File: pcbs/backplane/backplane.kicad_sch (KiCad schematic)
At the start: 138 parts, among them J1 Conn_01x02, J10 AFBR-2624Z, J11 AFBR-2624Z, J12 AFBR-1624Z, J14 Conn_01x02, J17 Conn_01x02, J19 Conn_01x02, J22 Conn_01x02, J24 Conn_01x02, J27 Conn_01x02, J29 Conn_01x02, J32 Conn_01x02, J34 Conn_01x02, J37 Conn_01x02, J39 Conn_01x02, J42 Conn_01x02, J44 Conn_01x02, J47 Conn_01x02, J48 Conn_01x02, J5 AFBR-2624Z, J8 Conn_01x02, J9 AFBR-2624Z, Q12 MMBT3904, Q13 MMBT3904, U11 AFBR-5972Z, U27 74LVC1G14, U29 74LVC1G14, U30 74LVC1G14, U32 LMV331, U7 FIN1019MTC

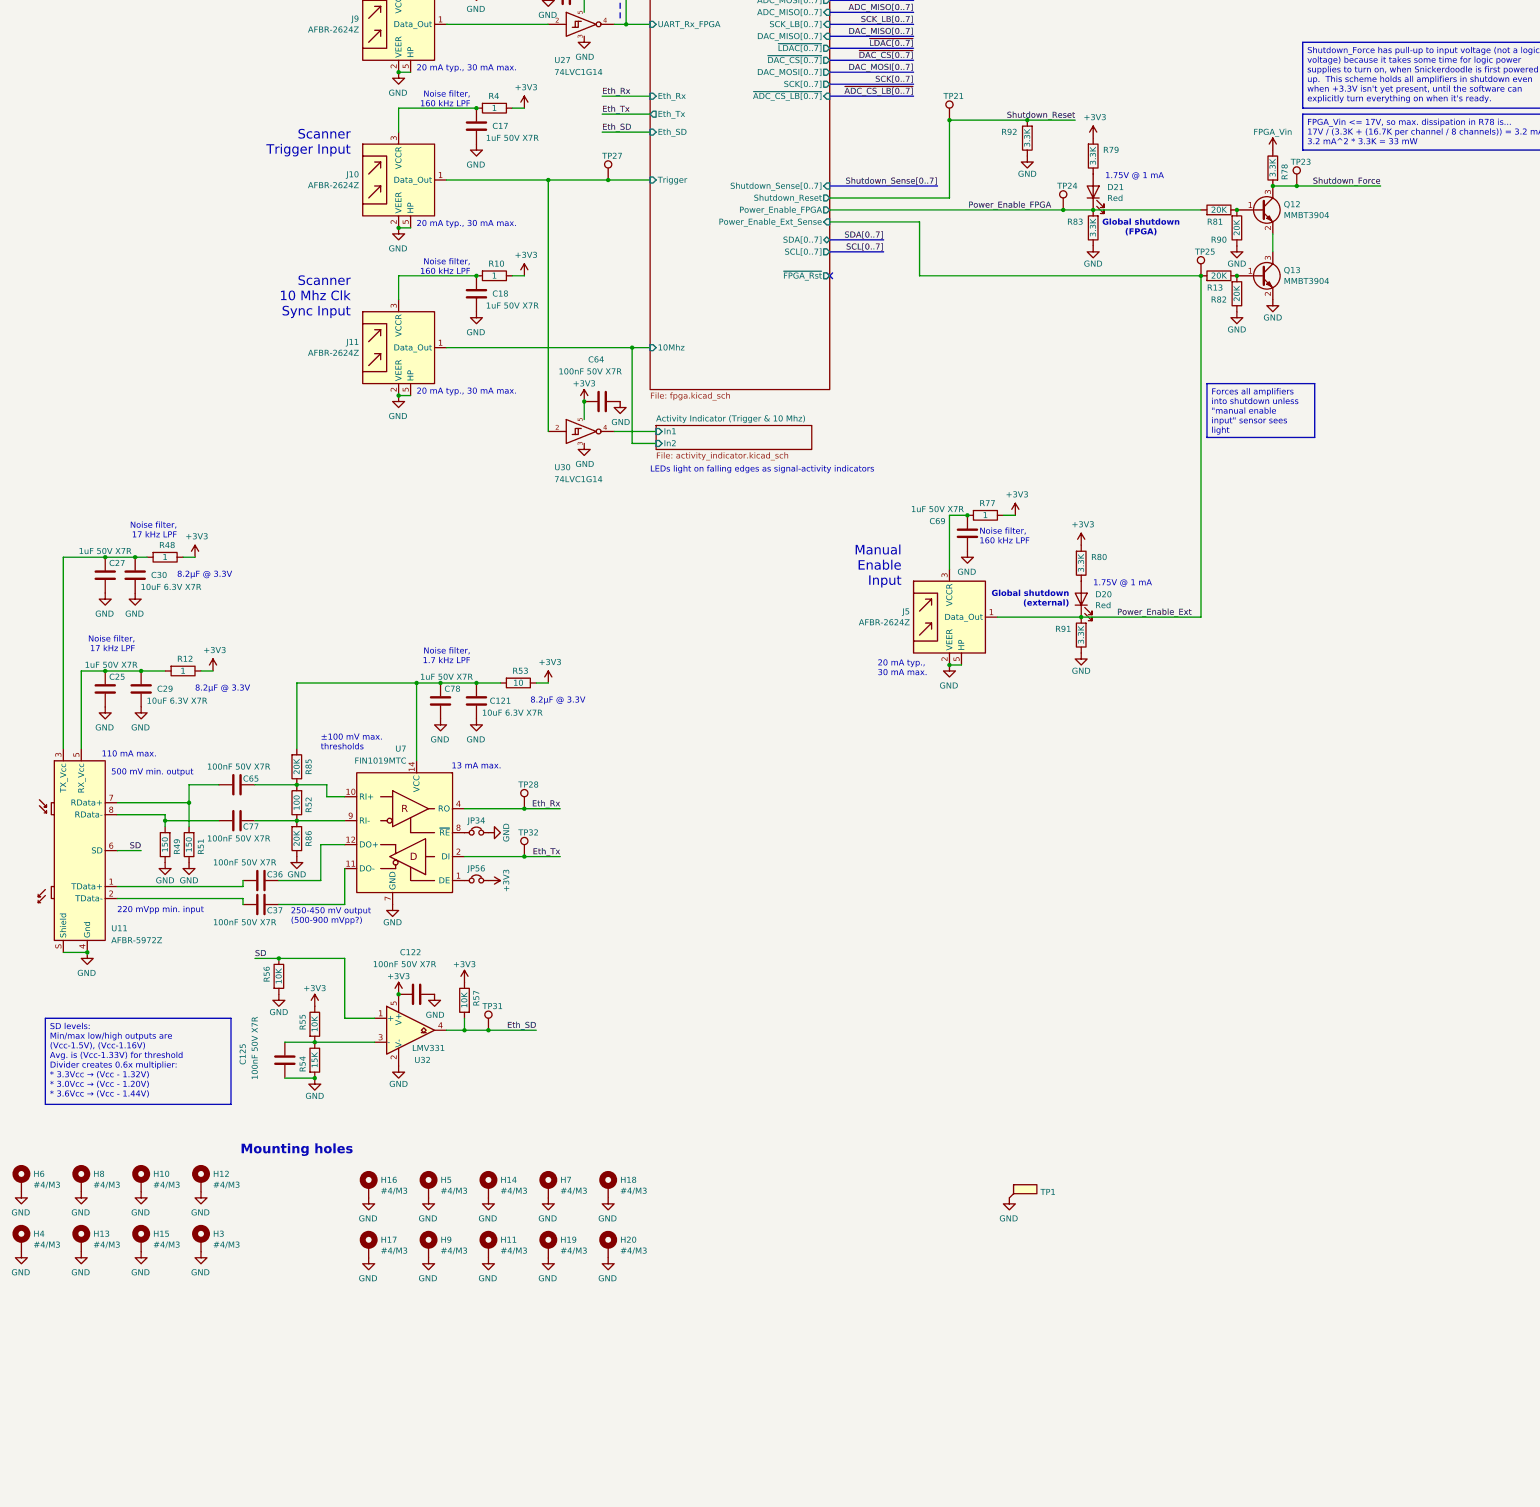
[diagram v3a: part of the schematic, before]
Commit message: Added dedicated Ethernet PHY IC to backplane
Backplane: added DP83822 PHY IC, instead of relying on FPGA's PL for PHY logic (fixes #44)
Libraries: added DP83822 symbol & footprint
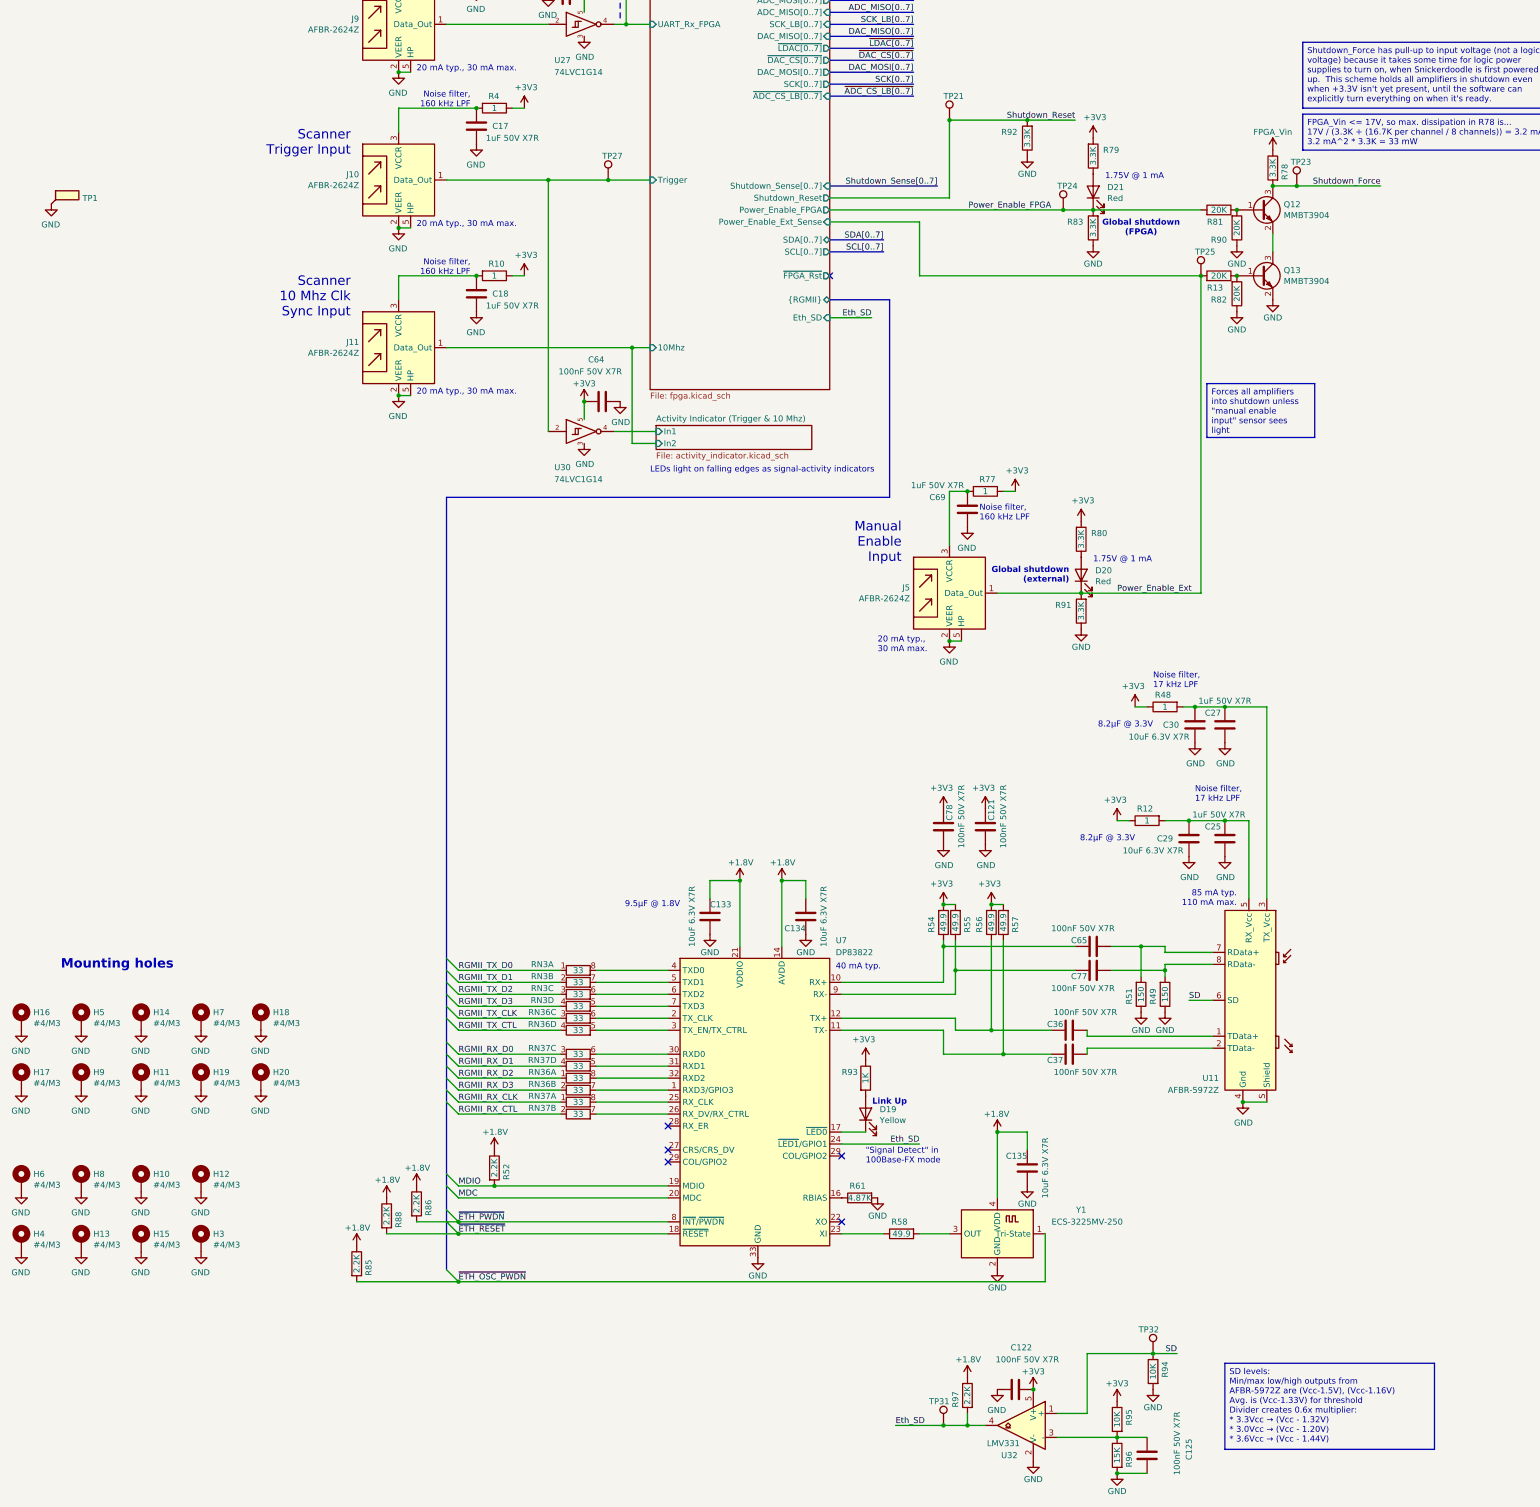
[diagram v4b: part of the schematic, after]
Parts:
- removed JP34, JP56: Jumper_NC_Small, Jumper:SolderJumper-2_P1.3mm_Bridged_RoundedPad1.0x1.5mm, symbol backplane-rescue:Jumper_NC_Small-Device
- removed R53: 10, Resistor_SMD:R_0805_2012Metric, symbol Device:R
- removed TP28: TestPoint, TestPoint:TestPoint_Pad_D1.0mm, symbol Connector:TestPoint
- removed U7: FIN1019MTC, Package_SO:TSSOP-14_4.4x5mm_P0.65mm, symbol Interface:FIN1019MTC
- added C133, C134, C135: 10uF 6.3V X7R, Capacitor_SMD:C_0805_2012Metric, symbol Device:C
- added D19: Yellow, LED_SMD:LED_0805_2012Metric, symbol Device:LED
- added R58: 49.9, Resistor_SMD:R_0805_2012Metric, symbol Device:R
- added R61: 4.87K, Resistor_SMD:R_0805_2012Metric, symbol Device:R
- added R88, R97: 2.2K, Resistor_SMD:R_0805_2012Metric, symbol Device:R
- added R93: 1K, Resistor_SMD:R_0805_2012Metric, symbol Device:R
- added R94, R95: 10K, Resistor_SMD:R_0805_2012Metric, symbol Device:R
- added R96: 15K, Resistor_SMD:R_0805_2012Metric, symbol Device:R
- added RN3, RN36, RN37: 33, Resistor_SMD:R_Array_Convex_4x0603, symbol Device:R_Pack04_Split
- added U7: DP83822, shim:Texas_RHB0032B_VQFN-32-1EP_5x5mm_P0.5mm_EP2.9x2.9mm, symbol shim:DP83822
- added Y1: ECS-3225MV-250, Crystal:Crystal_SMD_3225-4Pin_3.2x2.5mm, symbol Oscillator:ECS-2520MV-xxx-xx
- C121: value 10uF 6.3V X7R -> 100nF 50V X7R; footprint Capacitor_SMD:C_0805_2012Metric -> Capacitor_SMD:C_0603_1608Metric; MPN C0805C106K9RACTU -> C0603C104K5RACTU
- C78: value 1uF 50V X7R -> 100nF 50V X7R; footprint Capacitor_SMD:C_0805_2012Metric -> Capacitor_SMD:C_0603_1608Metric; MPN C0805C105K3RACTU -> C0603C104K5RACTU
- R52: value 100 -> 2.2K; MPN RK73H2ATTD1000F -> RK73H2ATTD2201F
- R54: value 15K -> 49.9; MPN RK73H2ATTD1502F -> RK73H2ATTD49R9F
- R55, R56, R57: value 10K -> 49.9; MPN RK73H2ATTD1002F -> RK73H2ATTD49R9F
- R85, R86: value 20K -> 2.2K; MPN RK73H2ATTD2002F -> RK73H2ATTD2201F
- TP32: footprint TestPoint:TestPoint_Pad_D1.0mm -> TestPoint:TestPoint_Pad_D2.0mm
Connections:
- net Eth_Tx is gone; now on net SD: TP32.1
- net +3V3: now also C121.1, C78.1, R54.2, R55.2, R56.2, R57.2, R93.1, R95.1; no longer R55.1, R57.1
- net Eth_SD: now also R97.2, U7.24 (~{LED1}/GPIO1); no longer R57.2
- net GND: now also C121.2, C78.2, C133.1, C134.1, C135.1, R61.2, R94.2, R96.2, U7.33 (GND), Y1.2 (GND); no longer C121.1, C78.1, R54.2, R56.2, R86.1
- net SD: now also R94.1; no longer R56.1
- net at C125.2, U32.3 (-): now also R95.2, R96.1; no longer R54.1, R55.2
- net at C37.1: now also R57.1, U7.11 (TX-)
- net at C36.1: now also R56.1, U7.12 (TX+)
- new net: RN3.6 (R3.2), U7.6 (TXD2)
- new net: RN36.5 (R4.2), U7.3 (TX_EN/TX_CTRL)
- new net: RN36.7 (R2.2), U7.1 (RXD3/GPIO3)
- new net: C65.1, R54.1, U7.10 (RX+)
- new net: R61.1, U7.16 (RBIAS)
- new net: D19.1 (K), U7.17 (~{LED0})
- new net: RN36.6 (R3.2), U7.2 (TX_CLK)
- new net: R58.1, U7.23 (XI)
- new net: RN37.8 (R1.2), U7.25 (RX_CLK)
- new net: RN37.7 (R2.2), U7.26 (RX_DV/RX_CTRL)
- new net: RN37.6 (R3.2), U7.30 (RXD0)
- new net: RN37.5 (R4.2), U7.31 (RXD1)
- new net: RN36.8 (R1.2), U7.32 (RXD2)
- new net: RN3.8 (R1.2), U7.4 (TXD0)
- new net: RN3.7 (R2.2), U7.5 (TXD1)
- new net: RN3.5 (R4.2), U7.7 (TXD3)
- new net: C77.1, R55.1, U7.9 (RX-)
- new net: D19.2 (A), R93.2
- new net: R58.2, Y1.3 (OUT)
- new net +1.8V: C133.2, C134.2, C135.2, R52.1, R85.1, R86.1, R88.1, R97.1, U7.14 (AVDD), U7.21 (VDDIO), Y1.4 (VDD)
- new net MDC: U7.20 (MDC)
- new net MDIO: R52.2, U7.19 (MDIO)
- new net RGMII_RX_CLK: RN37.1 (R1.1)
- new net RGMII_RX_CTL: RN37.2 (R2.1)
- new net RGMII_RX_D0: RN37.3 (R3.1)
- new net RGMII_RX_D1: RN37.4 (R4.1)
- new net RGMII_RX_D2: RN36.1 (R1.1)
- new net RGMII_RX_D3: RN36.2 (R2.1)
- new net RGMII_TX_CLK: RN36.3 (R3.1)
- new net RGMII_TX_CTL: RN36.4 (R4.1)
- new net RGMII_TX_D0: RN3.1 (R1.1)
- new net RGMII_TX_D1: RN3.2 (R2.1)
- new net RGMII_TX_D2: RN3.3 (R3.1)
- new net RGMII_TX_D3: RN3.4 (R4.1)
- new net ~{ETH_OSC_PWDN}: R85.2, Y1.1 (Tri-State)
- new net ~{ETH_PWDN}: R86.2, U7.8 (~{INT}/~{PWDN})
- new net ~{ETH_RESET}: R88.2, U7.18 (~{RESET})
- no-connect marks 1 -> 6
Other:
- sheet FPGA Board, Signal Distribution ports: added {RGMII}; removed Eth_Rx, Eth_Tx
- note added: ""Signal Detect" in 100Base-FX mode"
- note added: "40 mA typ."
- note added: "85 mA typ. 110 mA max."
- note added: "9.5µF @ 1.8V"
- note added: "Link Up"
- note removed: "110 mA max."
- note removed: "13 mA max."
- note removed: "220 mVpp min. input"
- note removed: "250-450 mV output (500-900 mVpp?)"
- note removed: "500 mV min. output"
- note removed: "Noise filter, 1.7 kHz LPF"
- note removed: "±100 mV max. thresholds"
- moved on the sheet: C25, C27, C29, C30, C36, C37, C65, C69, C77, D20, H11, H14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
